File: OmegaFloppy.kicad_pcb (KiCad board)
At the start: 2 copper layers, 22 x 42 mm, 20 parts, among them J1 DIN-6, J2 USB_C_Receptacle_USB2.0_16P, J3 AVR-ISP-6, U1 ATmega32U2-M, U2 74LS06, U3 TPD2EUSB30, Y1 16 MHz

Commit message: added project link
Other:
- board text added: "github.com/fastjack/OmegaFloppy"
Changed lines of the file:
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@@
+		)
+	)
+	(gr_text "github.com/fastjack/OmegaFloppy"
+		(at 179.5 76.7 90)
+		(layer "B.SilkS")
+		(effects
+			(font
+				(size 0.762 0.762)
+			)
+			(justify left bottom mirror)
 		)
 	)

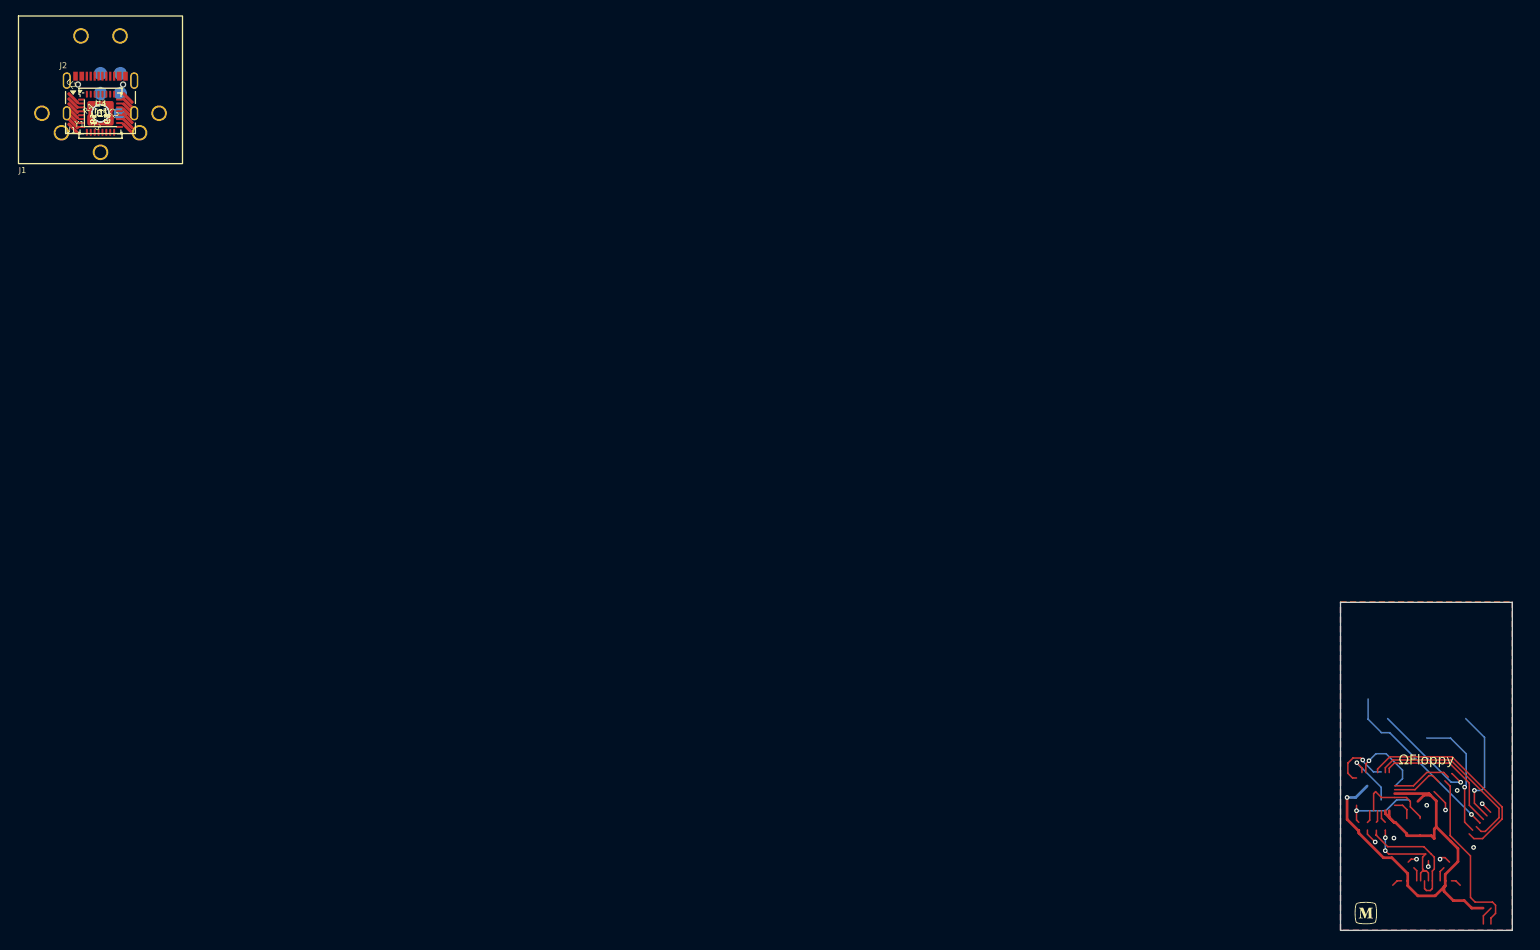
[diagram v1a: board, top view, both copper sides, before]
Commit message: fixed missing connection on IEC port
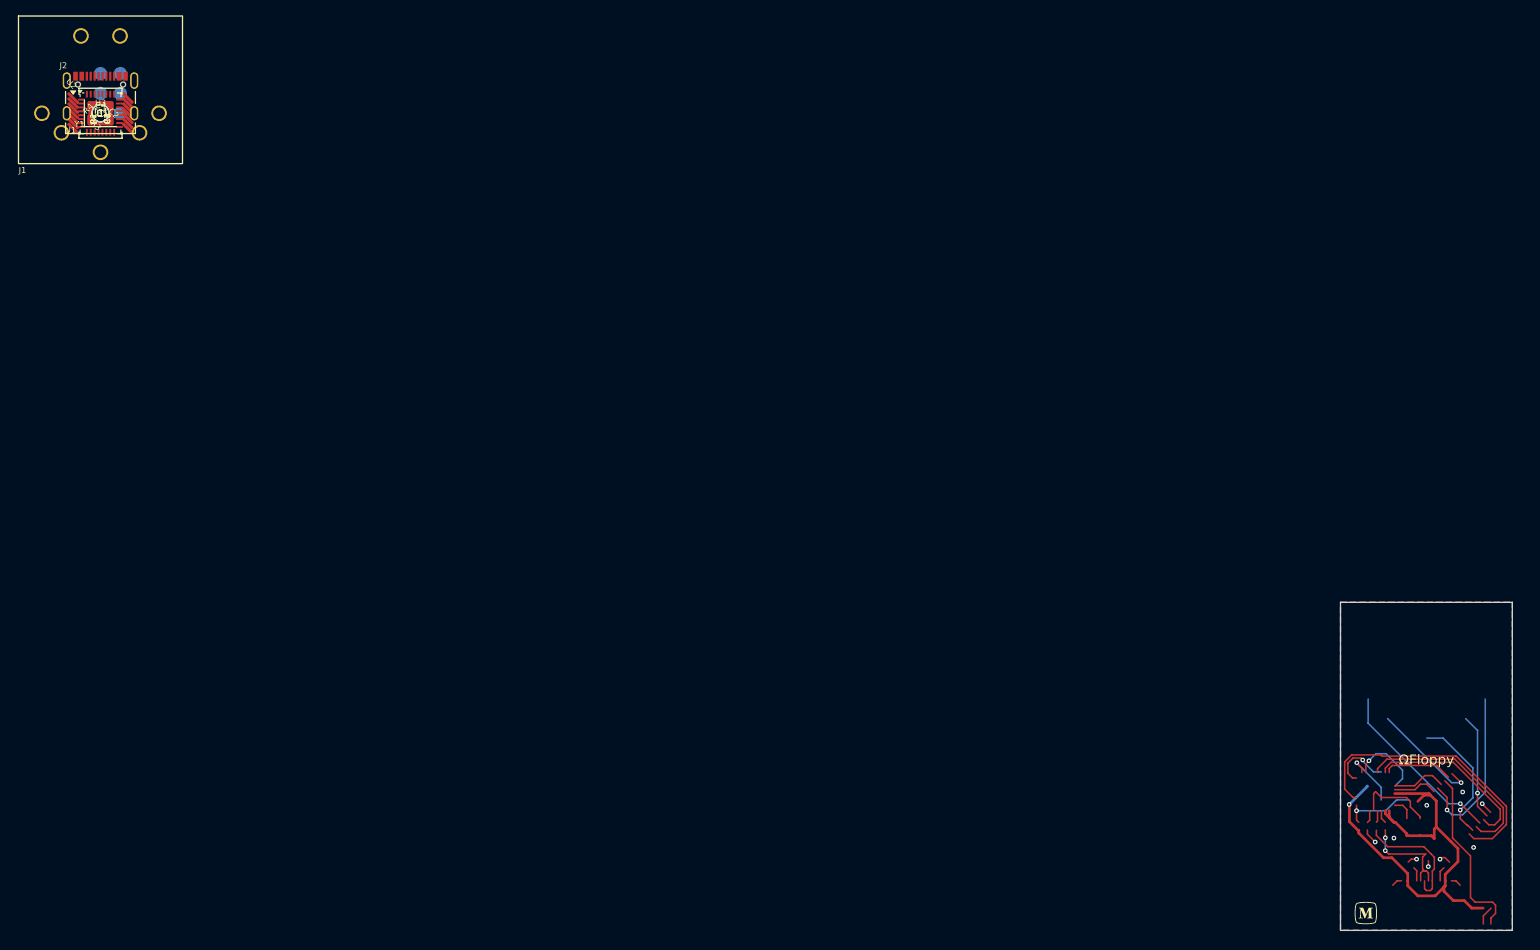
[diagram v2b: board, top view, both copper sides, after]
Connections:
- net /~{C2} renamed /~{ACT_LED}
- net /~{D0} renamed /~{IEC_CLK}
- net /~{D3} renamed /~{IEC_DATA}
- net /~{D4} renamed /~{IEC_SRQ}
- net /~{D6} renamed /~{IEC_RESET}
- net Net-(U3-D+) renamed /D+
- net Net-(U3-D-) renamed /D-
- J1 pad 3: GND -> /~{IEC_ATN}
- U1 pad 10: /D4 -> /IEC_DATA
- U1 pad 12: /D6 -> /IEC_SRQ
- U1 pad 22: unconnected-(U1-PC7-Pad22) -> /IRC_RESET
- U1 pad 5: /C2 -> /IEC_ATN
- U1 pad 6: /D0 -> /ACT_LED
- U1 pad 9: /D3 -> /IEC_CLK
- U2 pad 1: /D6 -> /IRC_RESET
- U2 pad 11: /C2 -> /ACT_LED
- U2 pad 12: unconnected-(U2-Pad12) -> /~{IEC_ATN}
- U2 pad 13: GND -> /IEC_ATN
- U2 pad 3: /D4 -> /IEC_SRQ
- U2 pad 5: /D3 -> /IEC_DATA
- U2 pad 9: /D0 -> /IEC_CLK
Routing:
- net /IRC_RESET: track 0.00 -> 37.4 mm
- net /D6: track 26.8 -> 0.00 mm
- net /IEC_SRQ: track 0.00 -> 25.8 mm
- net /D4: track 23.3 -> 0.00 mm
- net /IEC_DATA: track 0.00 -> 22.1 mm
- net /~{IEC_ATN}: track 0.00 -> 21.6 mm, vias 0 -> 1
- net /D3: track 17.6 -> 0.00 mm
- net /IEC_CLK: track 0.00 -> 8.88 mm
- net /D0: track 7.85 -> 0.00 mm
- net /ACT_LED: track 0.00 -> 6.97 mm
- net /C2: track 6.78 -> 0.00 mm
- net /IEC_ATN: track 0.00 -> 5.73 mm
- net GND: track 23.0 -> 20.0 mm, vias 10 -> 9
- net /~{IEC_DATA}: track 15.2 -> 13.6 mm
- net VCC: track 62.8 -> 61.9 mm
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
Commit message: added missing input pins
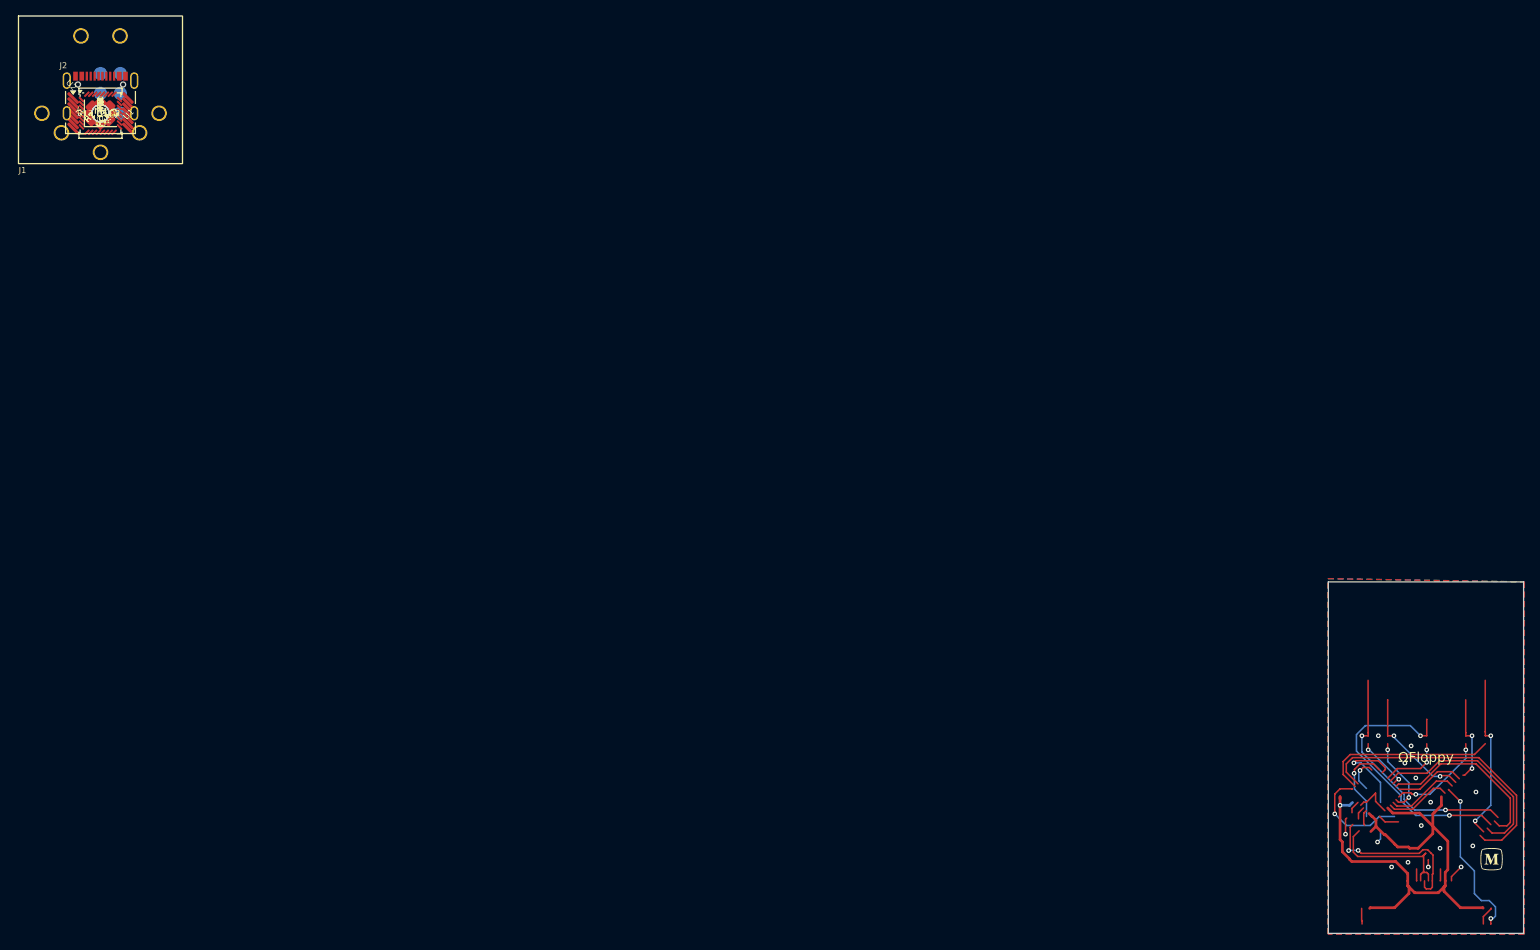
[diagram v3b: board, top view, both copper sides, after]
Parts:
- added D2: Power (green), LED_SMD:LED_0402_1005Metric, F.Cu at (0.00, 0.00)
- added R10, R11, R7, R8, R9: 100 k, Resistor_SMD:R_0402_1005Metric, F.Cu at (0.00, 0.00)
- added R12: 220, Resistor_SMD:R_0402_1005Metric, F.Cu at (0.00, 0.00)
- D1: value LED -> Activity (red)
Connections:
- net /IEC_CLK renamed /IO_DATA
- net /IEC_DATA renamed /IO_SRQ
- net /IEC_SRQ renamed /IO_RESET
- net /IRC_RESET renamed /IO_ATN
- J1 pad 1: /~{IEC_SRQ} -> /~{IO_SRQ}
- J1 pad 3: /~{IEC_ATN} -> /~{IO_ATN}
- J1 pad 4: /~{IEC_CLK} -> /~{IO_CLK}
- J1 pad 5: /~{IEC_DATA} -> /~{IO_DATA}
- J1 pad 6: /~{IEC_RESET} -> /~{IO_RESET}
- U1 pad 11: unconnected-(U1-PD5-Pad11) -> /IO_SRQ_IN
- U1 pad 13: unconnected-(U1-~{HWB}/PD7-Pad13) -> /IO_RESET_IN
- U1 pad 23: unconnected-(U1-PC6-Pad23) -> /IO_ATN_IN
- U1 pad 5: /IEC_ATN -> /ACT_LED
- U1 pad 6: /ACT_LED -> /IO_CLK
- U1 pad 7: unconnected-(U1-PD1-Pad7) -> /IO_CLK_IN
- U1 pad 8: unconnected-(U1-PD2-Pad8) -> /IO_DATA_IN
- U2 pad 10: /~{ACT_LED} -> /~{IO_CLK}
- U2 pad 11: /ACT_LED -> /IO_CLK
- U2 pad 12: /~{IEC_ATN} -> /~{ACT_LED}
- U2 pad 13: /IEC_ATN -> /ACT_LED
- U2 pad 2: /~{IEC_RESET} -> /~{IO_ATN}
- U2 pad 4: /~{IEC_SRQ} -> /~{IO_RESET}
- U2 pad 6: /~{IEC_DATA} -> /~{IO_SRQ}
- U2 pad 8: /~{IEC_CLK} -> /~{IO_DATA}
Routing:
- net /~{IO_RESET}: track 0.00 -> 35.8 mm, vias 0 -> 2
- net /~{IO_SRQ}: track 0.00 -> 31.3 mm, vias 0 -> 2
- net /IO_ATN_IN: track 0.00 -> 23.0 mm
- net /~{IEC_SRQ}: track 22.7 -> 0.00 mm, vias 1 -> 0
- net /~{IEC_ATN}: track 21.6 -> 0.00 mm, vias 1 -> 0
- net /~{IO_ATN}: track 0.00 -> 21.4 mm, vias 0 -> 2
- net /~{IEC_RESET}: track 16.9 -> 0.00 mm, vias 1 -> 0
- net /~{IO_CLK}: track 0.00 -> 16.0 mm, vias 0 -> 2
- net /~{IEC_CLK}: track 14.5 -> 0.00 mm, vias 1 -> 0
- net /~{IEC_DATA}: track 13.6 -> 0.00 mm, vias 1 -> 0
- net /IO_DATA_IN: track 0.00 -> 12.7 mm, vias 0 -> 2
- net /~{IO_DATA}: track 0.00 -> 11.1 mm, vias 0 -> 2
- net VCC: track 61.9 -> 72.1 mm
- net /IO_CLK_IN: track 0.00 -> 10.0 mm, vias 0 -> 2
- net /IO_CLK: track 0.00 -> 9.32 mm
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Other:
- board size 22 x 42 mm -> 25 x 45 mm
